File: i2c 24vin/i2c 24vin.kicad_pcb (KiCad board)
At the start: 2 copper layers, 123.2 x 50.2 mm, 109 parts, among them IC1 PCF8575PWR, J1 Conn_01x04, J10 power in, J2 Conn_01x04, J3 Conn_01x04, J4 Conn_01x04, J5 Conn_01x01, J6 Conn_01x01, J7 qwiic 1, J8 qwiic 2, J9 i2c test points, U1 PC817, U10 PC817, U11 PC817, U12 PC817, U13 PC817, U14 PC817, U15 PC817, U16 PC817, U2 PC817, U3 PC817, U4 PC817, U5 PC817, U6 PC817, U7 PC817, U8 PC817, U9 PC817

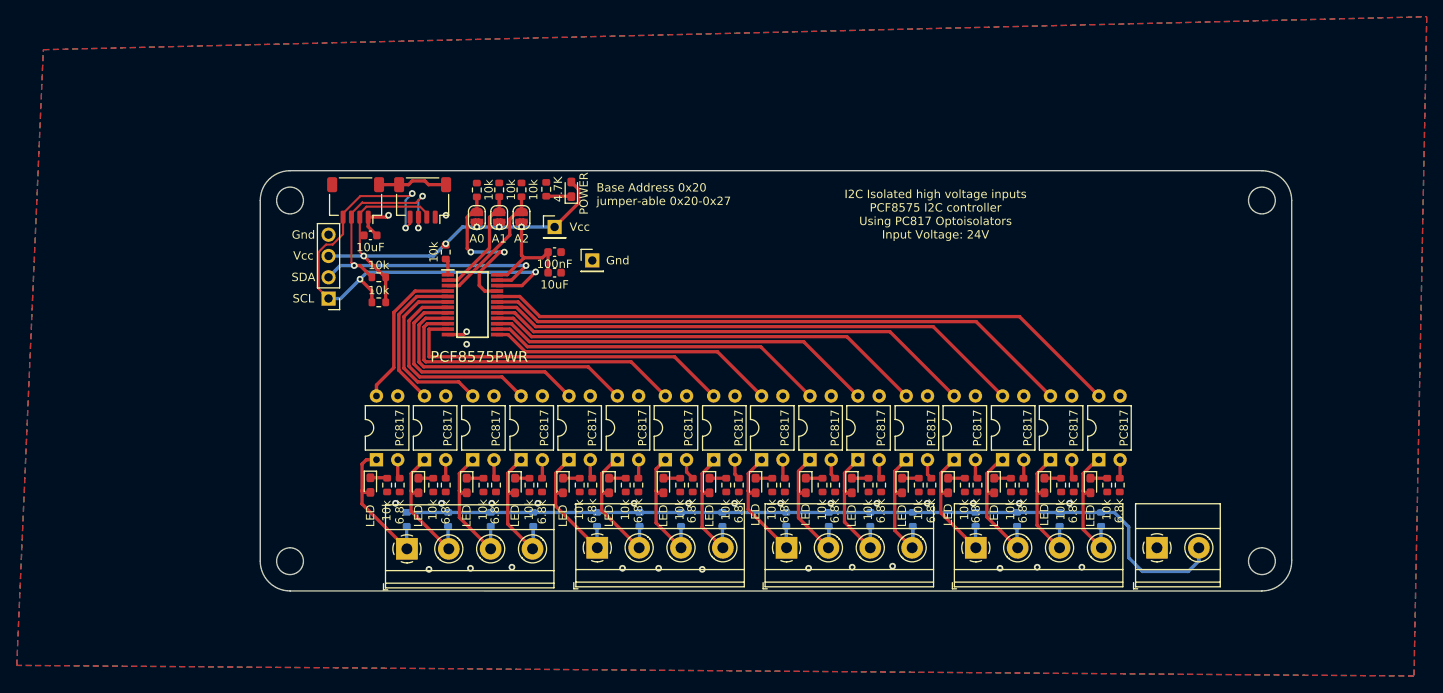
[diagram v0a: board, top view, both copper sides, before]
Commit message: DFM 24vin
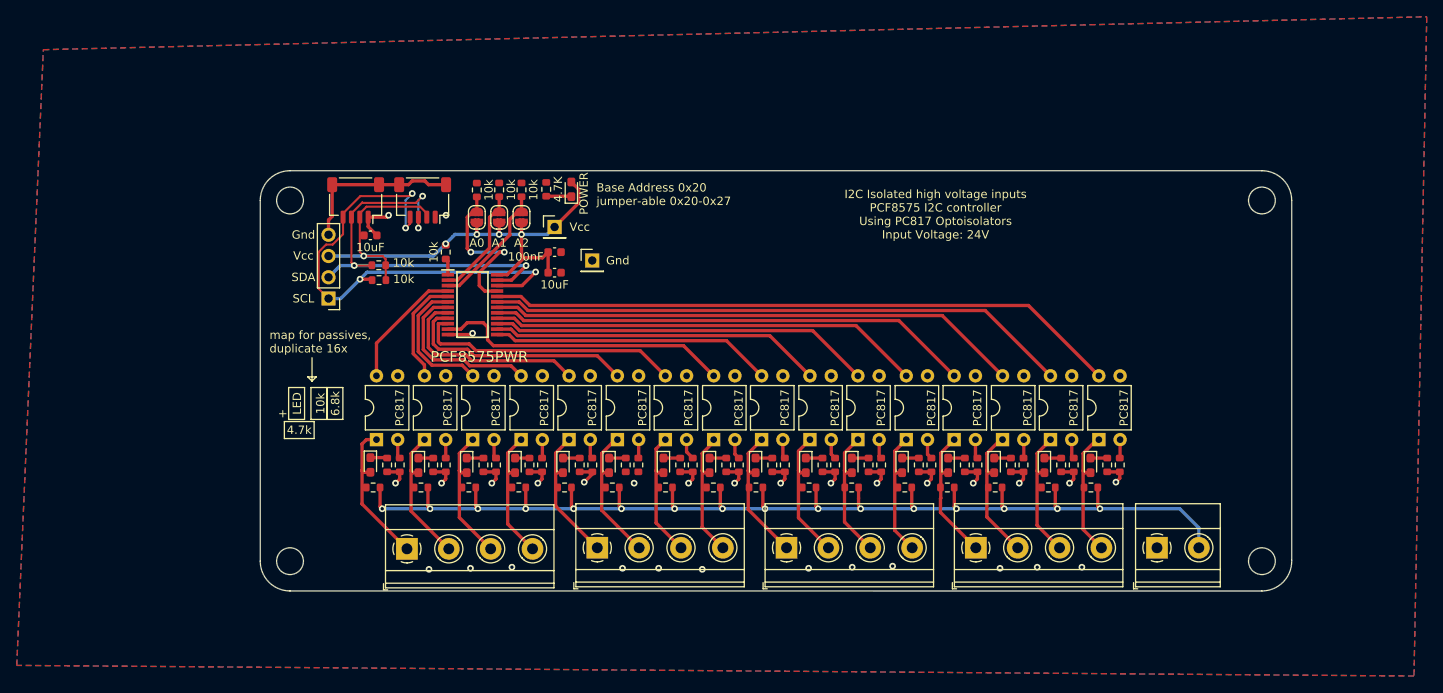
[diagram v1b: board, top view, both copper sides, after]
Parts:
- R40, R41, R42, R43, R44, R45, R46, R47, R48, R49, R50, R51, R52, R53, R54, R55: moved to F.Cu
- moved R41 5.52 mm to (104.3, 118.1), turned to 180 degrees
- moved R40 5.43 mm to (127.2, 118.1), turned to 180 degrees
- moved R49 5.26 mm to (150.1, 118.1), turned to 180 degrees
- moved R48 5.08 mm to (172.9, 118.1), turned to 180 degrees
- moved R42 5.00 mm to (110.0, 118.1), turned to 180 degrees
- moved R45 5.00 mm to (132.9, 118.1), turned to 180 degrees
- moved R53 4.61 mm to (178.6, 118.1), turned to 180 degrees
- moved R43 4.61 mm to (115.8, 118.1), turned to 180 degrees
- moved R50 4.48 mm to (156.4, 118.1), turned to 180 degrees
- moved R51 4.41 mm to (161.5, 118.1), turned to 180 degrees
- moved R46 4.23 mm to (139.3, 118.1), turned to 180 degrees
- moved R44 4.18 mm to (121.7, 118.1), turned to 180 degrees
- moved R54 4.04 mm to (185.0, 118.1), turned to 180 degrees
- moved R55 4.00 mm to (190.1, 118.1), turned to 180 degrees
- moved R47 3.96 mm to (145.0, 118.1), turned to 180 degrees
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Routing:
- net GND: track 15.9 -> 74.1 mm, vias 30 -> 31
- net +24V: track 101.8 -> 143.1 mm, vias 0 -> 16
- net input7: track 41.5 -> 35.6 mm
- net input2: track 21.7 -> 16.2 mm
- net input6: track 37.6 -> 32.1 mm
- net input5: track 33.6 -> 28.1 mm
- net input3: track 25.6 -> 20.2 mm
- net input4: track 29.6 -> 24.2 mm
- net input1: track 17.7 -> 13.0 mm
- net input0: track 18.3 -> 15.0 mm
- net /scl: track 62.2 -> 60.4 mm
- net VCC: track 69.9 -> 71.3 mm
- net input9: track 40.7 -> 39.7 mm
- net input15: track 76.8 -> 75.8 mm
- net input10: track 46.7 -> 45.7 mm
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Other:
- board text added: "+"
- board text added: "map for passives, duplicate 16x"
